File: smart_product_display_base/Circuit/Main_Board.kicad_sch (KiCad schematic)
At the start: 43 parts, among them Q1 BD681, Q2 BD681, Q3 BD681, Q4 BD681, Q5 BD681, Q6 BD681, U1 PC817, U2 PC817, U3 PC817, U4 PC817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

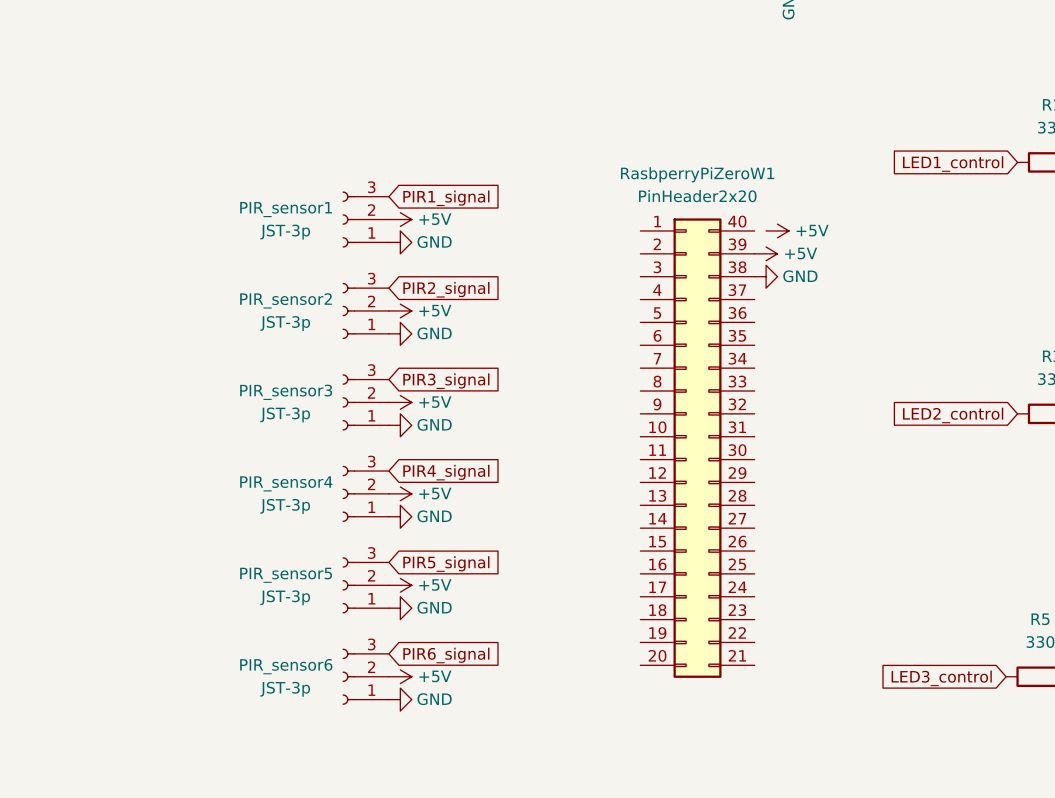
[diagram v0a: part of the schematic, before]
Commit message: tested Power circuit and finished most PCB layout
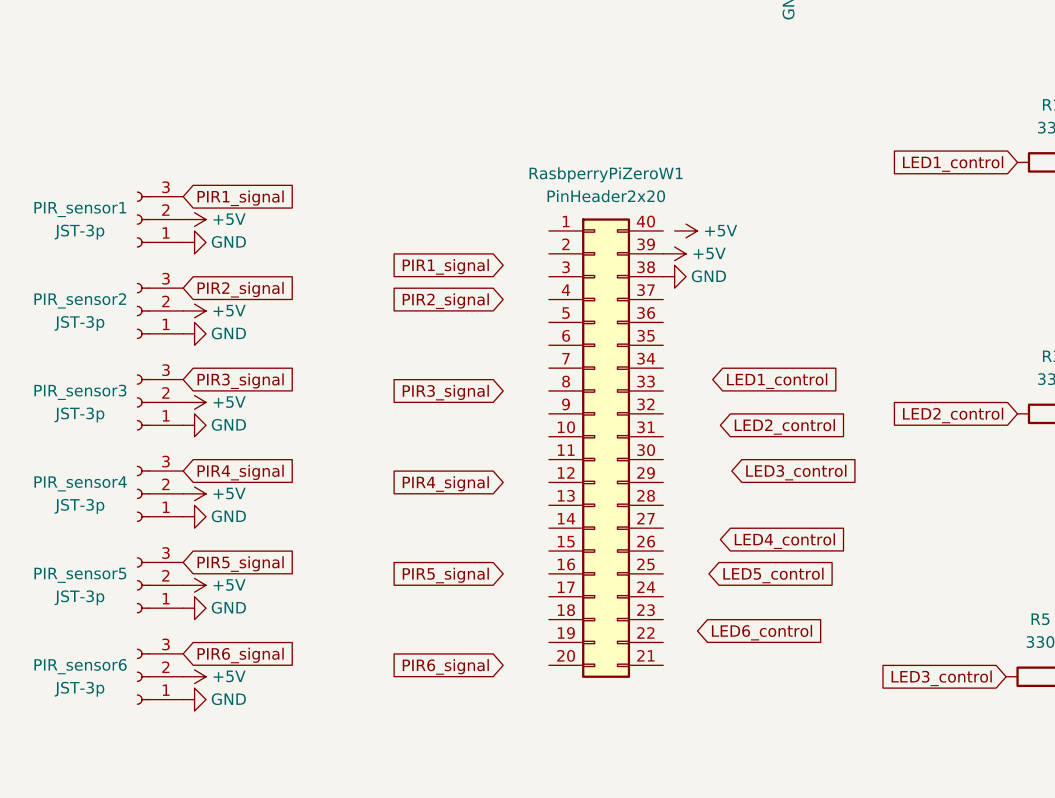
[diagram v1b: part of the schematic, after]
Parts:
- C1: footprint (none) -> Capacitor_THT:CP_Radial_D8.0mm_P3.50mm
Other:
- moved on the sheet: PIR_sensor1, PIR_sensor2, PIR_sensor3, PIR_sensor4, PIR_sensor5, PIR_sensor6, RasbperryPiZeroW1

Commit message: finished PCB layout
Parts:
- removed H1, H4: MountingHole, MountingHole:MountingHole_5.5mm_Pad_TopBottom, symbol Mechanical:MountingHole
- removed LED5, LED6: JST-2p, Connector_JST:JST_EH_B2B-EH-A_1x02_P2.50mm_Vertical, symbol Connector:Conn_01x02_Socket
- removed PIR_sensor5, PIR_sensor6: JST-3p, Connector_JST:JST_EH_B3B-EH-A_1x03_P2.50mm_Vertical, symbol Connector:Conn_01x03_Socket
- removed Q5, Q6: BD681, Package_TO_SOT_THT:TO-126-3_Vertical, symbol Device:Q_NPN_Darlington_BCE
- removed RasbperryPiZeroW1: PinHeader2x20, Connector_PinSocket_2.54mm:PinSocket_2x20_P2.54mm_Vertical, symbol Connector_Generic:Conn_02x20_Counter_Clockwise
- removed U5, U6: PC817, Package_DIP:DIP-4_W7.62mm, symbol Isolator:PC817
- added H5, H6: MountingHole, MountingHole:MountingHole_2.5mm_Pad_TopOnly, symbol Mechanical:MountingHole
- added R13, R15: 10k, Resistor_THT:R_Axial_DIN0207_L6.3mm_D2.5mm_P7.62mm_Horizontal, symbol Device:R
- added R14, R16: 20k, Resistor_THT:R_Axial_DIN0207_L6.3mm_D2.5mm_P7.62mm_Horizontal, symbol Device:R
- added RaspberryPiZeroW1: Conn_02x20, Connector_PinSocket_2.54mm:PinSocket_2x20_P2.54mm_Vertical, symbol Connector_Generic:Conn_02x20_Odd_Even
- H2, H3: footprint MountingHole:MountingHole_5.5mm_Pad_TopBottom -> MountingHole:MountingHole_4mm_Pad_TopOnly
- R11: value 1k -> 10k
- R12: value 1k -> 20k
- R8: value 330 -> 10k
- R9: value 330 -> 20k
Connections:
- net LED5_control is gone; now on net PIR1_signal: R8.1
- net LED6_control is gone; now on net GND: R9.1
- net +5V: now also PIR_sensor1.1 (Pin_1), PIR_sensor2.1 (Pin_1), PIR_sensor3.1 (Pin_1), PIR_sensor4.1 (Pin_1), RaspberryPiZeroW1.1 (Pin_1), RaspberryPiZeroW1.3 (Pin_3); no longer PIR_sensor1.2 (Pin_2), PIR_sensor2.2 (Pin_2), PIR_sensor3.2 (Pin_2), PIR_sensor4.2 (Pin_2), R11.2, R12.2
- net GND: now also PIR_sensor1.2 (Pin_2), PIR_sensor2.2 (Pin_2), PIR_sensor3.2 (Pin_2), PIR_sensor4.2 (Pin_2), R12.1, R14.1, R16.1, RaspberryPiZeroW1.5 (Pin_5); no longer PIR_sensor1.1 (Pin_1), PIR_sensor2.1 (Pin_1), PIR_sensor3.1 (Pin_1), PIR_sensor4.1 (Pin_1)
- net LED1_control: now also RaspberryPiZeroW1.11 (Pin_11)
- net LED2_control: now also RaspberryPiZeroW1.15 (Pin_15)
- net LED3_control: now also RaspberryPiZeroW1.17 (Pin_17)
- net LED4_control: now also RaspberryPiZeroW1.23 (Pin_23)
- net PIR1_signal: now also R9.2, RaspberryPiZeroW1.25 (Pin_25); no longer PIR_sensor1.3 (Pin_3)
- net PIR2_signal: now also R11.1, R12.2, RaspberryPiZeroW1.21 (Pin_21); no longer PIR_sensor2.3 (Pin_3)
- net PIR3_signal: now also R13.1, R14.2, RaspberryPiZeroW1.35 (Pin_35); no longer PIR_sensor3.3 (Pin_3)
- net PIR4_signal: now also R15.1, R16.2, RaspberryPiZeroW1.37 (Pin_37); no longer PIR_sensor4.3 (Pin_3)
- net at R8.2: now also PIR_sensor1.3 (Pin_3)
- new net: PIR_sensor4.3 (Pin_3), R15.2
- new net: PIR_sensor2.3 (Pin_3), R11.2
- new net: PIR_sensor3.3 (Pin_3), R13.2
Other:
- moved on the sheet: C1, LED1, LED2, LED3, LED4, PIR_sensor1, PIR_sensor2, PIR_sensor3, PIR_sensor4, PowerIn1, Q1, Q2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
